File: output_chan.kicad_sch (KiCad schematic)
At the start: 12 parts, among them U4 MAX14917AFM+

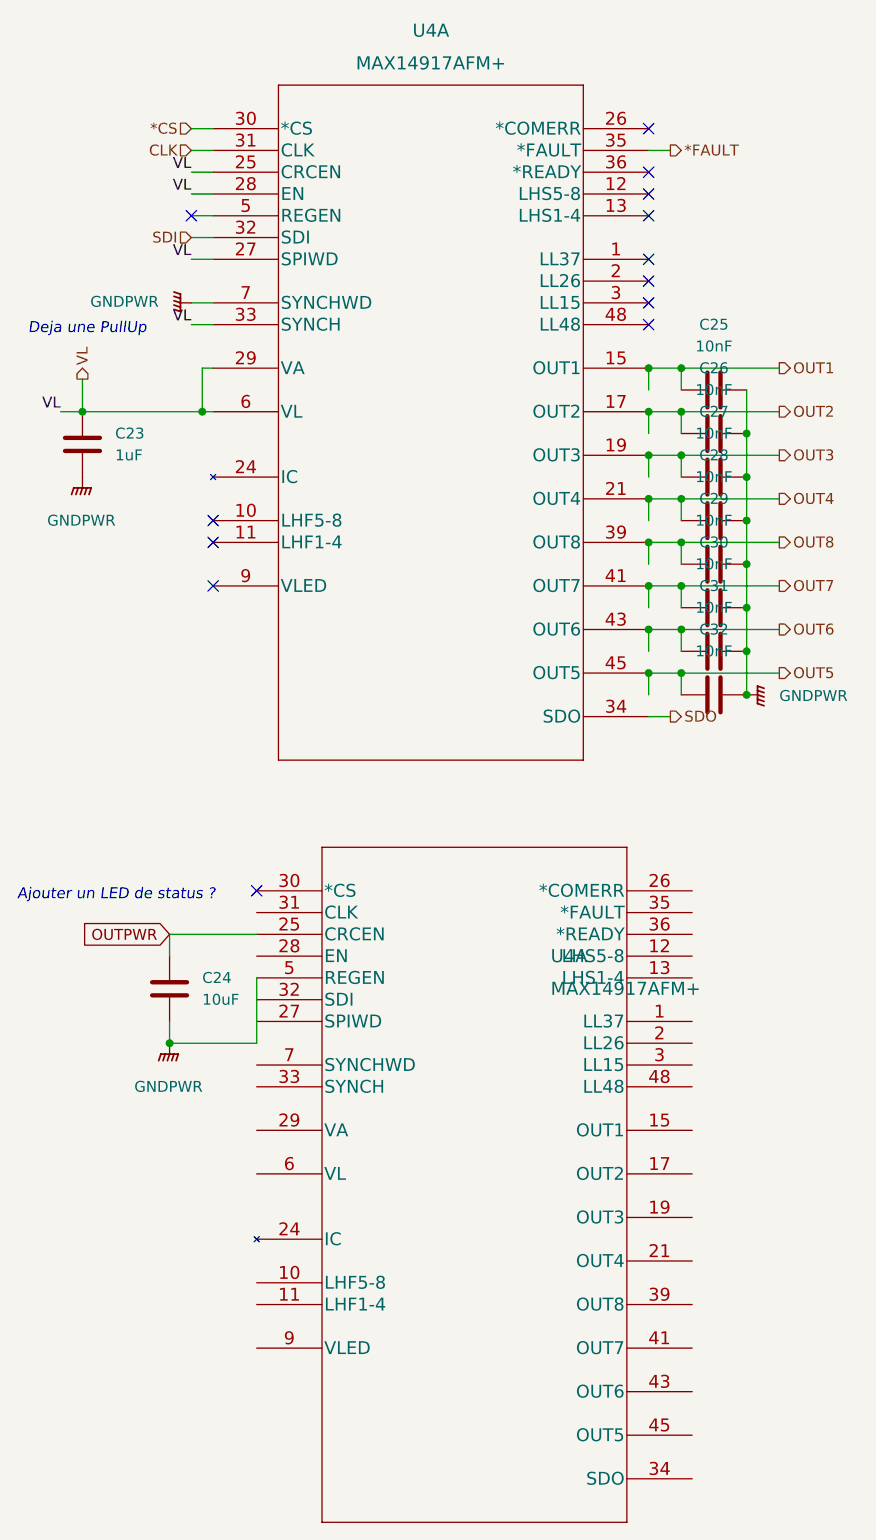
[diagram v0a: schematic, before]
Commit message: move MPG to dedicated file
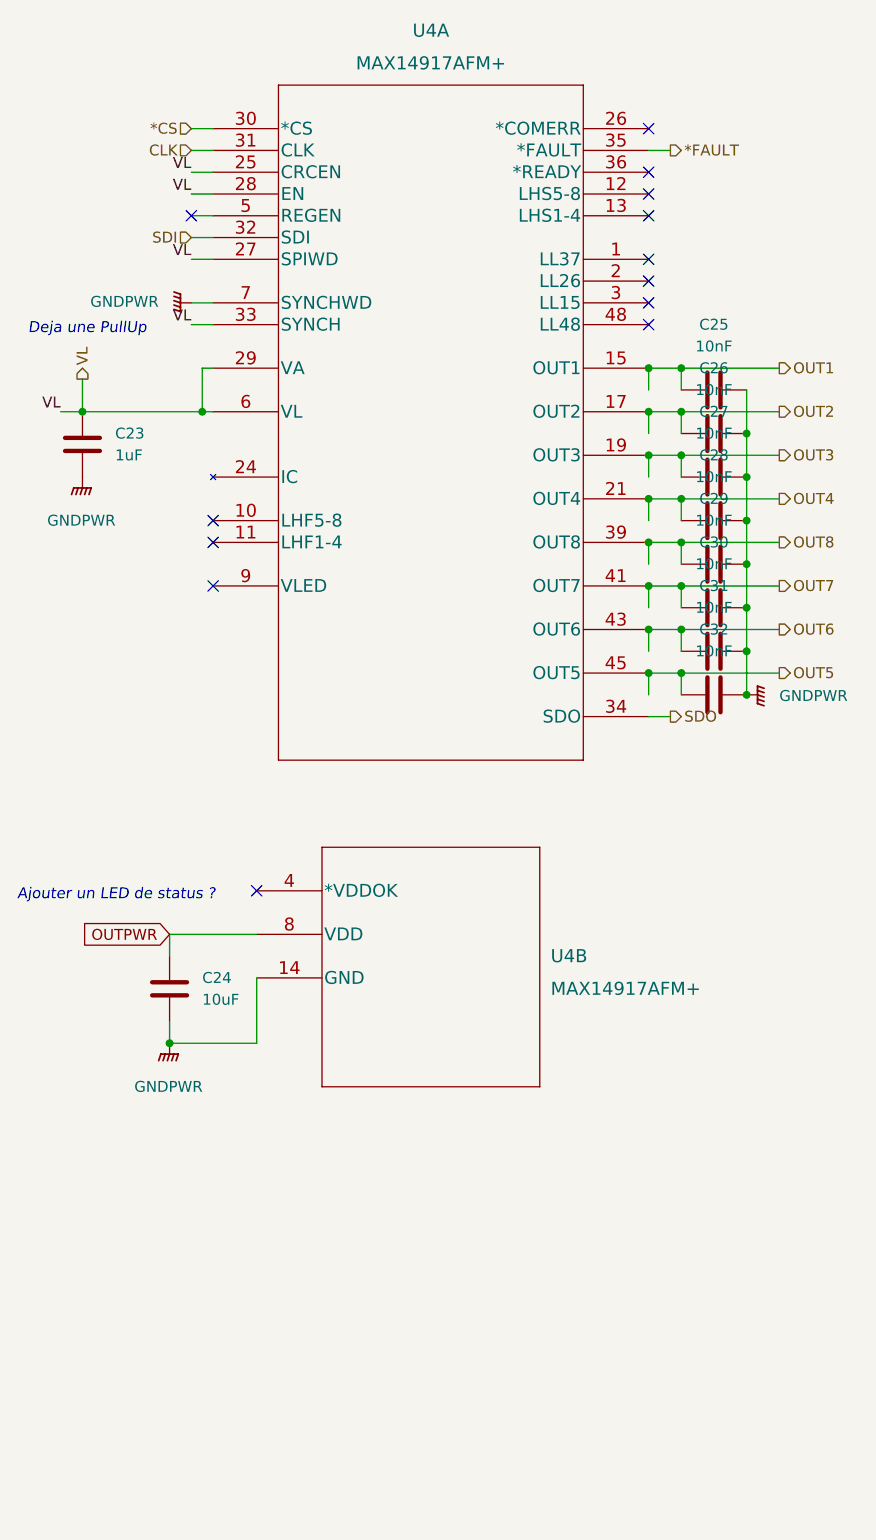
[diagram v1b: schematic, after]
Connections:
- net GNDPWR: now also U4.14 (GND), U4.23 (GND), U4.38 (GND), U4.47 (GND); no longer U4.5 (REGEN)
- net OUTPWR: now also U4.49 (EPAD), U4.8 (VDD); no longer U4.25 (CRCEN)

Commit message: fix warnings
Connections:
- net GNDPWR: now also U4.5 (REGEN); no longer U4.14 (GND), U4.23 (GND), U4.38 (GND), U4.47 (GND)
- net OUTPWR: now also U4.25 (CRCEN); no longer U4.49 (EPAD), U4.8 (VDD)
- new net: U4.15 (OUT1), U4.16 (OUT1)
- new net: U4.17 (OUT2), U4.18 (OUT2)
- new net: U4.19 (OUT3), U4.20 (OUT3)
- new net: U4.21 (OUT4), U4.22 (OUT4)
- new net: U4.37 (VL), U4.6 (VL)
- new net: U4.39 (OUT8), U4.40 (OUT8)
- new net: U4.41 (OUT7), U4.42 (OUT7)
- new net: U4.43 (OUT6), U4.44 (OUT6)
- new net: U4.45 (OUT5), U4.46 (OUT5)
